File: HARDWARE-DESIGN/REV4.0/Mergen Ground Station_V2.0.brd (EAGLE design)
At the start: 83.8 x 62.2 mm, 87 parts, among them J2 CON-SD-CARD_MICROSD-2908-05, J4 U.FL, U13 L86, U15 AMS1117-5V, U16 AMS1117-3.3, X2 JST-XH-04-PIN-LONG-PAD, Y1 ABMM2-8.000MHZ-E2-T

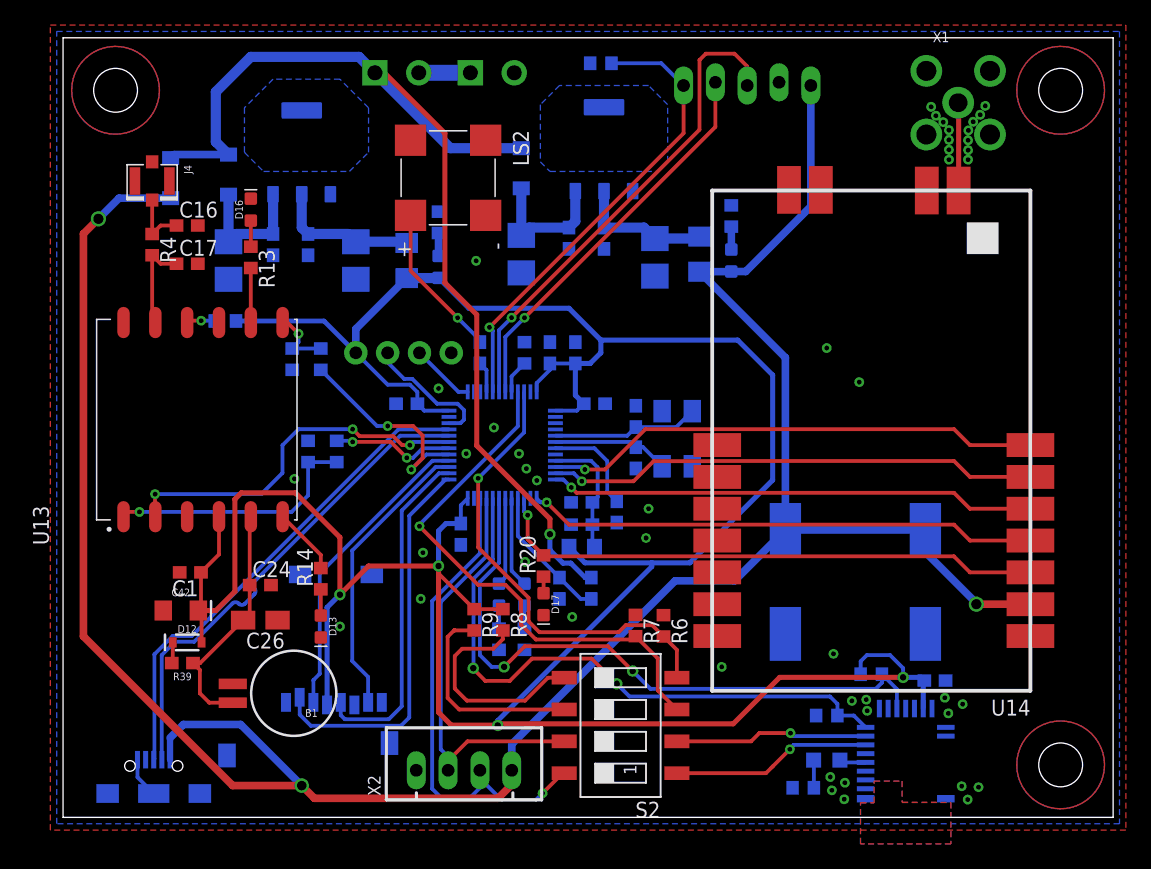
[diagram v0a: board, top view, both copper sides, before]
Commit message: Lora configuration connectors were added
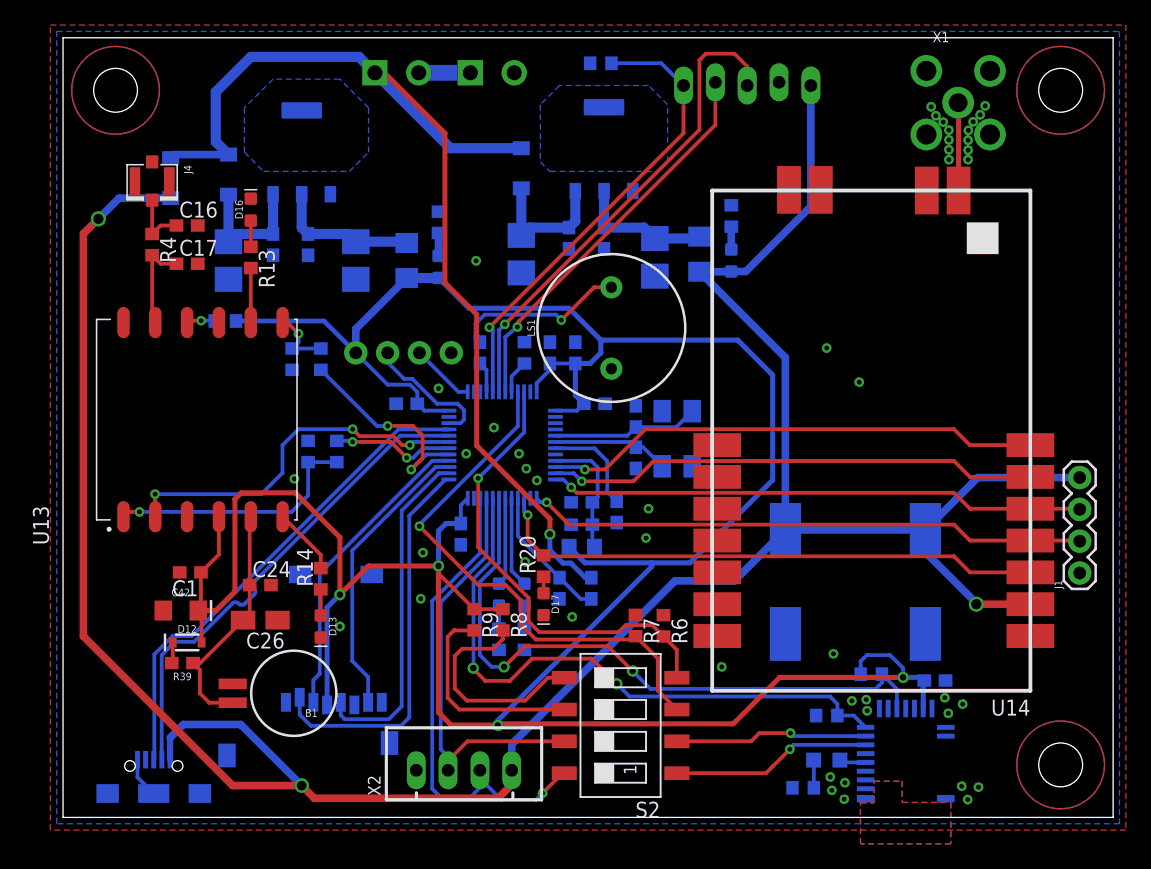
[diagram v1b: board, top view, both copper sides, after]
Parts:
- removed LS2: CMT-7525S-SMT, CMT-7525S-SMT:CUI_CMT-7525S-SMT
- added J1: (no value), SparkFun-Connectors:1X04
- added LS1: BUZZER-PTH, SparkFun-Electromechanical:BUZZER-12MM
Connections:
- net 5V: now also J1.4
- net GND: now also J1.1, LS1.-; no longer LS2.N
- net N$4: now also LS1.+; no longer LS2.P
- net RX2: now also J1.2
- net TX2: now also J1.3
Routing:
- net 5V: track 194.4 -> 208.4 mm
- net TX2: track 38.9 -> 42.8 mm
- net RX2: track 40.8 -> 44.8 mm
- net N$4: track 12.4 -> 14.0 mm
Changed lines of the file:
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@@
 <attribute name="VALUE" x="51.526" y="34.388" size="1.27" layer="28" rot="MR270" align="top-left"/>
-</element>
-<element name="LS2" library="CMT-7525S-SMT" package="CUI_CMT-7525S-SMT" value="CMT-7525S-SMT" x="30.988" y="51.816" smashed="yes" rot="R270">
-<attribute name="AVAILABILITY" value="In Stock" x="45.466" y="63.5" size="1.778" layer="27" rot="R270" display="off"/>
-<attribute name="CUI_PURCHASE_URL" value="https://www.cuidevices.com/product/audio/buzzers/audio-transducers/cmt-7525s-smt-tr?utm_source=snapeda.com&amp;utm_medium=referral&amp;utm_campaign=snapedaBOM" x="45.466" y="63.5" size="1.778" layer="27" rot="R270" display="off"/>
-<attribute name="DESCRIPTION" value="7.5 mm, 3.6 Vo-p, 90 dB, Surface Mount (SMT), Magnetic Audio Transducer Buzzer" x="45.466" y="63.5" size="1.778" layer="27" rot="R270" display="off"/>
-<attribute name="MF" value="CUI Devices" x="45.466" y="63.5" size="1.778" layer="27" rot="R270" display="off"/>
-<attribute name="MP" value="CMT-7525S-SMT-TR" x="45.466" y="63.5" size="1.778" layer="27" rot="R270" display="off"/>
-<attribute name="NAME" x="36.164140625" y="55.620509375" size="1.271509375" layer="25" rot="R270"/>
-<attribute name="PACKAGE" value=" CUI Inc." x="45.466" y="63.5" size="1.778" layer="27" rot="R270" display="off"/>
-<attribute name="PRICE" value="None" x="45.466" y="63.5" size="1.778" layer="27" rot="R270" display="off"/>
-<attribute name="VALUE" x="24.381459375" y="55.62776875" size="1.271259375" layer="27" rot="R270"/>
 </element>
 <element name="U1" library="ELTASSAN" package="MDBT42T-AT" value="" x="67.6148" y="4.7498" smashed="yes" rot="MR180">
@@
 <attribute name="VALUE" x="10.4688" y="51.7906" size="1.27" layer="28" rot="MR270" align="top-center"/>
 <attribute name="ZENER_VOLTAGE" value="" x="8.8392" y="51.7906" size="1.778" layer="28" rot="MR270" display="off"/>
+</element>
+<element name="LS1" library="SparkFun-Electromechanical" library_urn="urn:adsk.eagle:library:516" package="BUZZER-12MM" package3d_urn="urn:adsk.eagle:package:38558/1" value="BUZZER-PTH" x="44.0182" y="39.8272" smashed="yes" rot="R90">
+<attribute name="NAME" x="37.9222" y="39.8272" size="0.6096" layer="25" font="vector" ratio="20" rot="R90" align="bottom-center"/>
+<attribute name="PROD_ID" value="COMP-08253" x="30.988" y="27.813" size="1.778" layer="27" rot="R90" display="off"/>
+<attribute name="SF_SKU" value="COM-07950" x="30.988" y="27.813" size="1.778" layer="27" rot="R90" display="off"/>
+<attribute name="VALUE" x="38.4302" y="39.8272" size="0.6096" layer="27" font="vector" ratio="20" rot="R90" align="top-center"/>
+</element>
+<element name="J1" library="SparkFun-Connectors" library_urn="urn:adsk.eagle:library:27162923" package="1X04" package3d_urn="urn:adsk.eagle:package:27162919/2" value="" x="81.407" y="20.2692" smashed="yes" rot="R90">
+<attribute name="NAME" x="80.01" y="18.9992" size="0.6096" layer="25" font="vector" ratio="20" rot="R90"/>
+<attribute name="PROD_ID" value="CONN-09696" x="81.407" y="20.2692" size="1.778" layer="27" rot="R90" display="off"/>
+<attribute name="VALUE" x="83.439" y="18.9992" size="0.6096" layer="27" font="vector" ratio="20" rot="R90"/>
 </element>
 </elements>
@@
 <via x="69.5452" y="57.4802" extent="1-16" drill="0.381"/>
 <via x="73.8632" y="57.5564" extent="1-16" drill="0.381"/>
-<contactref element="LS2" pad="N"/>
 <contactref element="R42" pad="2"/>
 <contactref element="R43" pad="2"/>
@@
 <via x="37.1348" y="21.1582" extent="1-16" drill="0.381"/>
 <via x="18.7198" y="27.7876" extent="1-16" drill="0.381"/>
+<contactref element="LS1" pad="-"/>
+<contactref element="J1" pad="1"/>
 </signal>
 <signal name="SWDIO">
@@
 <wire x1="13.7922" y1="3.302" x2="1.8796" y2="15.2146" width="0.6096" layer="1"/>
 <wire x1="1.8796" y1="15.2146" x2="1.8796" y2="47.3456" width="0.6096" layer="1"/>
+<contactref element="J1" pad="4"/>
+<wire x1="69.088" y1="23.708" x2="73.2692" y2="27.8892" width="0.6096" layer="16"/>
+<wire x1="73.2692" y1="27.8892" x2="81.407" y2="27.8892" width="0.6096" layer="16"/>
 </signal>
 <signal name="3.3V">
@@
 <wire x1="71.374" y1="26.67" x2="72.644" y2="25.4" width="0.3048" layer="1"/>
 <wire x1="72.644" y1="25.4" x2="77.47" y2="25.4" width="0.3048" layer="1"/>
+<contactref element="J1" pad="3"/>
+<wire x1="77.47" y1="25.4" x2="81.3562" y2="25.4" width="0.3048" layer="1"/>
+<wire x1="81.3562" y1="25.4" x2="81.407" y2="25.3492" width="0.3048" layer="1"/>
 </signal>
 <signal name="RX2">
@@
 <wire x1="77.47" y1="22.86" x2="72.644" y2="22.86" width="0.3048" layer="1"/>
 <wire x1="72.644" y1="22.86" x2="71.374" y2="24.13" width="0.3048" layer="1"/>
+<contactref element="J1" pad="2"/>
+<wire x1="77.47" y1="22.86" x2="81.3562" y2="22.86" width="0.3048" layer="1"/>
+<wire x1="81.3562" y1="22.86" x2="81.407" y2="22.8092" width="0.3048" layer="1"/>
 </signal>
 <signal name="MISO">
@@
 <contactref element="J3" pad="3"/>
 <wire x1="35.056" y1="34.73" x2="35.056" y2="39.65616875" width="0.3048" layer="16"/>
-<wire x1="35.056" y1="39.65616875" x2="36.05253125" y2="40.6527" width="0.3048" layer="16"/>
-<via x="36.05253125" y="40.6527" extent="1-16" drill="0.381"/>
-<wire x1="36.05253125" y1="40.6527" x2="51.054" y2="55.65416875" width="0.3048" layer="1"/>
+<wire x1="35.056" y1="39.65616875" x2="35.51913125" y2="40.1193" width="0.3048" layer="16"/>
+<via x="35.51913125" y="40.1193" extent="1-16" drill="0.381"/>
+<wire x1="35.51913125" y1="40.1193" x2="51.054" y2="55.65416875" width="0.3048" layer="1"/>
 <wire x1="51.054" y1="55.65416875" x2="51.054" y2="61.214" width="0.3048" layer="1"/>
 <wire x1="51.562" y1="61.722" x2="51.054" y2="61.214" width="0.3048" layer="1"/>
@@
 <contactref element="J3" pad="2"/>
 <wire x1="35.556" y1="34.73" x2="35.556" y2="39.112" width="0.3048" layer="16"/>
-<via x="37.084" y="40.64" extent="1-16" drill="0.381"/>
-<wire x1="37.084" y1="40.64" x2="52.324" y2="55.88" width="0.3048" layer="1"/>
-<wire x1="52.324" y1="55.88" x2="52.324" y2="59.436" width="0.3048" layer="1"/>
-<wire x1="35.556" y1="39.112" x2="37.084" y2="40.64" width="0.3048" layer="16"/>
+<via x="36.5252" y="39.9034" extent="1-16" drill="0.381"/>
+<wire x1="52.324" y1="56.0324" x2="36.6522" y2="40.3606" width="0.3048" layer="1"/>
+<wire x1="36.6522" y1="40.3606" x2="36.5252" y2="40.207140625" width="0.3048" layer="1"/>
+<wire x1="36.5252" y1="39.9034" x2="36.5252" y2="40.207140625" width="0.3048" layer="1"/>
+<wire x1="52.324" y1="56.0324" x2="52.324" y2="59.436" width="0.3048" layer="1"/>
+<wire x1="35.556" y1="39.112" x2="36.5252" y2="39.9034" width="0.3048" layer="16"/>
 </signal>
 <signal name="LED">
@@
 <contactref element="R20" pad="1"/>
 <wire x1="38.608" y1="19.978" x2="38.608" y2="18.657" width="0.3048" layer="1"/>
-</signal>
-<signal name="N$4">
-<contactref element="R32" pad="2"/>
-<wire x1="27.996" y1="44.394" x2="31.75" y2="40.64" width="0.3048" layer="1"/>
-<via x="31.75" y="40.64" extent="1-16" drill="0.381"/>
-<wire x1="33.528" y1="38.696" x2="33.528" y2="38.862" width="0.3048" layer="16"/>
-<wire x1="31.75" y1="40.64" x2="33.528" y2="38.862" width="0.3048" layer="16"/>
-<contactref element="LS2" pad="P"/>
-<wire x1="27.988" y1="48.816" x2="27.996" y2="48.808" width="0.3048" layer="1"/>
-<wire x1="27.996" y1="48.808" x2="27.996" y2="44.394" width="0.3048" layer="1"/>
 </signal>
 <signal name="D2">
@@
 <wire x1="31.5214" y1="13.6398" x2="32.1056" y2="14.224" width="0.3048" layer="1"/>
 </signal>
+<signal name="N$4">
+<contactref element="R32" pad="2"/>
+<contactref element="LS1" pad="+"/>
+<wire x1="33.528" y1="38.696" x2="33.1724" y2="39.0516" width="0.3048" layer="16"/>
+<wire x1="33.1724" y1="39.0516" x2="33.1724" y2="40.1574" width="0.3048" layer="16"/>
+<wire x1="33.1724" y1="40.1574" x2="33.909" y2="40.894" width="0.3048" layer="16"/>
+<wire x1="39.5986" y1="40.894" x2="40.0304" y2="40.4622" width="0.3048" layer="16"/>
+<via x="40.0304" y="40.4622" extent="1-16" drill="0.381"/>
+<wire x1="40.0304" y1="40.4622" x2="42.6454" y2="43.0772" width="0.3048" layer="1"/>
+<wire x1="42.6454" y1="43.0772" x2="44.0182" y2="43.0772" width="0.3048" layer="1"/>
+<wire x1="33.909" y1="40.894" x2="39.5986" y2="40.894" width="0.3048" layer="16"/>
+</signal>
 </signals>
